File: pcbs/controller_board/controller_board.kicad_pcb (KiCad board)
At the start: 2 copper layers, 72 x 44 mm, 41 parts, among them J1 RJ45, J2 PINHD-1X7, J3 PINHD-1X12, J4 PINHD-1X4, P1 24V / 5A, Q1 220mA / 50V, Q2 220mA / 50V, U1 8-28V in / 5V 5W out, U2 Particle2 / Boron, U3 A: 1.2 to 3.3V B: 1.8 to 5.5V

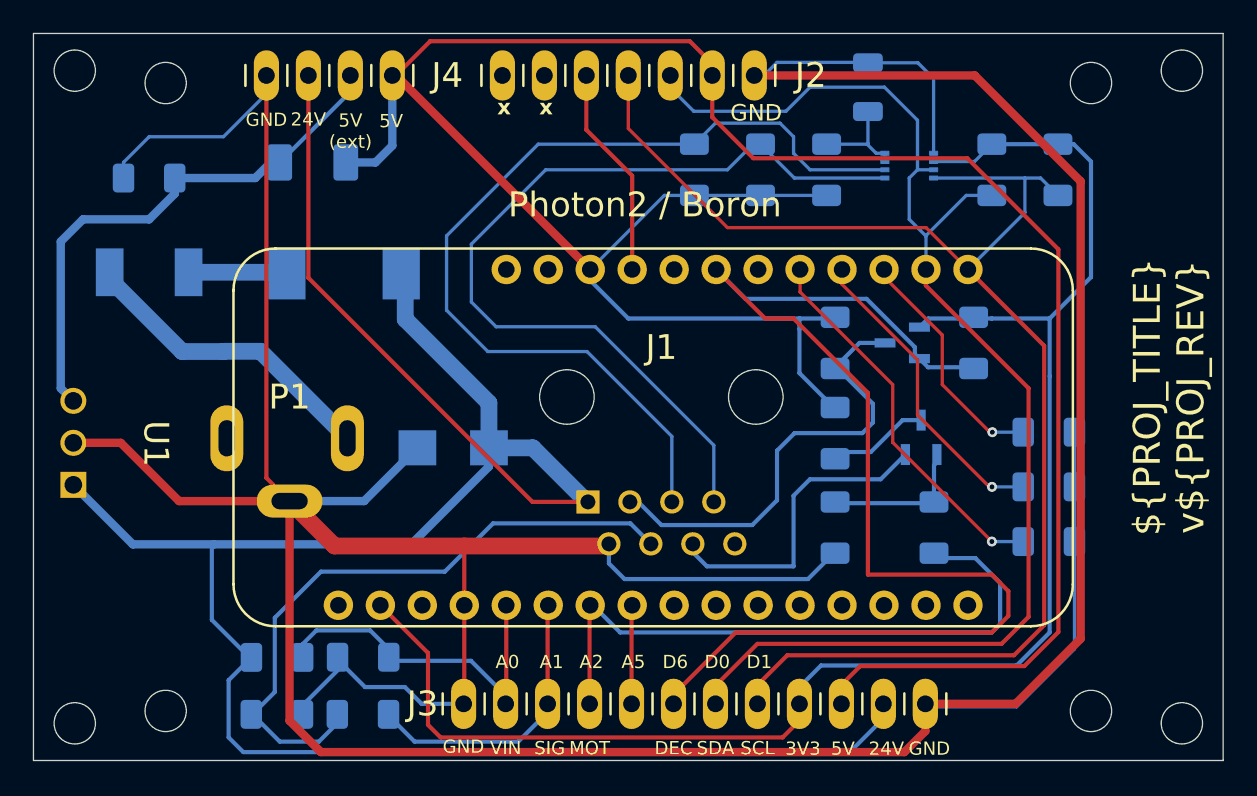
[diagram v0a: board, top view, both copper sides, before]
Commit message: update controller board to version 1.1 - i2c level shifting back to mosfets
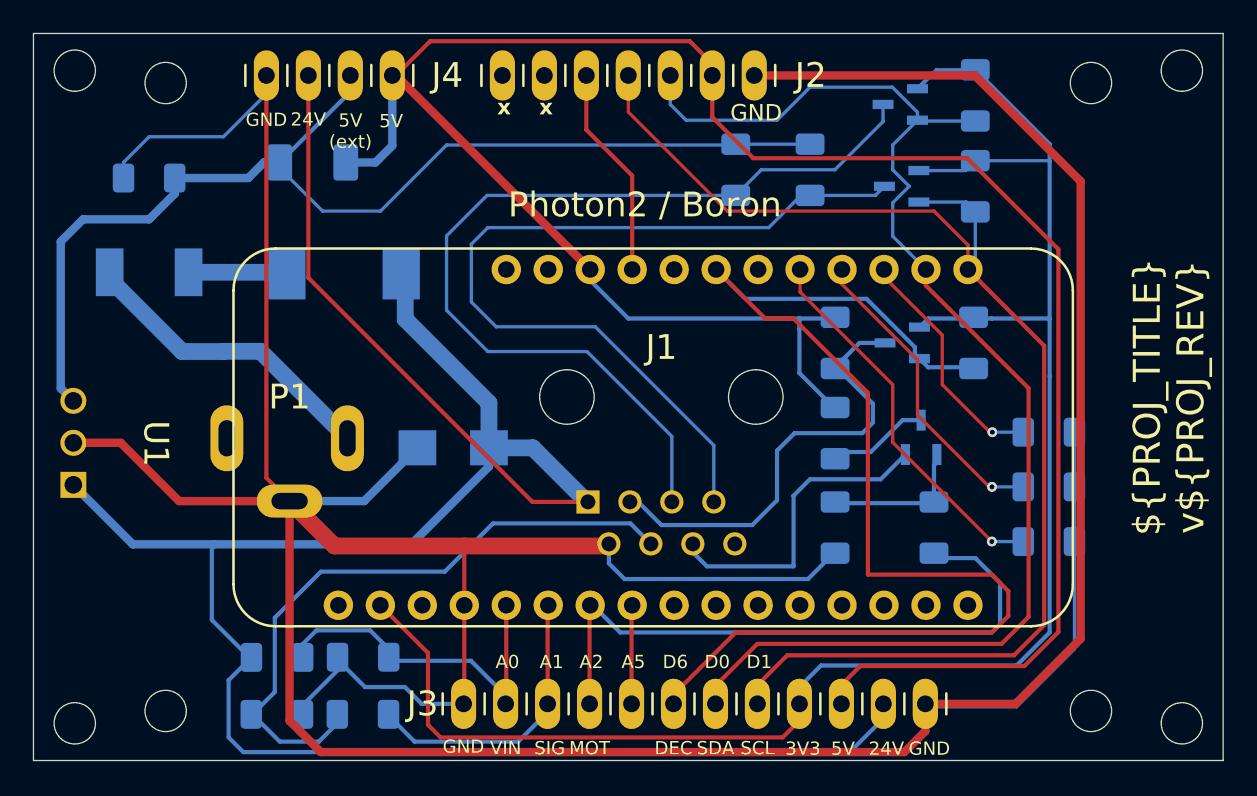
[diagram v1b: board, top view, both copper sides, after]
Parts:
- removed C1: 100pF, footprints:C_1206
- removed R15: 200kΩ, footprints:R_1206
- removed U3: A: 1.2 to 3.3V B: 1.8 to 5.5V, footprints:SOT-765-1_VSSOP8
- added Q3: 220mA / 50V, footprints:SOT-23-3, B.Cu at (152.5, 84.0)
- added Q4: 220mA / 50V, footprints:SOT-23-3, B.Cu at (152.5, 89.0)
- R11, R12, R13, R14: value 2.2kΩ -> 10kΩ
- moved R11 19.5 mm to (142.5, 88.0), turned to -90 degrees
- moved R14 13.0 mm to (157.0, 89.0), turned to 90 degrees
- moved R13 7.00 mm to (147.0, 88.0)
- moved R12 4.61 mm to (157.0, 83.5)
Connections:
- D2 pad 2: /Vout -> +5Vout
- J4 pad 3: /Vout -> +5Vout
- R11 pad 1: /D0-SDA -> +5Vout
- R11 pad 2: +3V3 -> /5V-SCL
- R13 pad 1: /5V-SCL -> +5Vout
- R13 pad 2: +5V -> /5V-SDA
- R14 pad 1: /5V-SDA -> /D0-SDA
- R14 pad 2: +5V -> +3V3
- R7 pad 1: /Vout -> +5Vout
- U1 pad 3: /Vout -> +5Vout
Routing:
- net +5Vout: track 0.00 -> 67.7 mm
- net /Vout: track 32.8 -> 0.00 mm
- net +5V: track 150.3 -> 134.2 mm
- net GND: track 277.2 -> 261.6 mm
- net +3V3: track 98.3 -> 106.4 mm
- net /D0-SDA: track 87.9 -> 80.7 mm
- net Net-(U3-EN): track 6.25 -> 0.00 mm
- net /5V-SDA: track 53.7 -> 52.5 mm
- net /5V-SCL: track 56.4 -> 55.6 mm
- net /D1-SCL: track 79.9 -> 80.4 mm

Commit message: use updated header symbols, otherwise no changes
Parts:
- J2: value PINHD-1X7 -> Conn_01x07
- J3: value PINHD-1X12 -> Conn_01x12
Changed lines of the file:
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@@
 	(net 37 "/S3")
 	(net 38 "/D3")
-	(net 39 "unconnected-(J2-Pad6)")
-	(net 40 "unconnected-(J2-Pad7)")
+	(net 39 "unconnected-(J2-Pin_6-Pad6)")
+	(net 40 "unconnected-(J2-Pin_7-Pad7)")
 	(net 41 "unconnected-(P1-Pad3)")
 	(net 42 "/A5")
@@
 			)
 		)
-		(property "Value" "PINHD-1X12"
+		(property "Value" "Conn_01x12"
 			(at -15.24 3.175 0)
 			(unlocked yes)
@@
 			)
 		)
-		(property "Datasheet" ""
+		(property "Datasheet" "~"
 			(at 0 0 0)
 			(layer "F.Fab")
@@
 			)
 		)
-		(property "Description" "PIN HEADER"
+		(property "Description" "Basic 0.1\" PTH"
 			(at 0 0 0)
 			(layer "F.Fab")
@@
 			)
 		)
+		(property ki_fp_filters "Connector*:*_1x??_*")
 		(sheetname "/")
 		(sheetfile "controller_board.kicad_sch")
@@
 			(remove_unused_layers no)
 			(net 1 "GND")
-			(pinfunction "1")
+			(pinfunction "Pin_1")
 			(pintype "passive")
 			(solder_mask_margin 0.1016)
@@
 			(remove_unused_layers no)
 			(net 4 "/A0-VIN")
-			(pinfunction "2")
+			(pinfunction "Pin_2")
 			(pintype "passive")
 			(solder_mask_margin 0.1016)
@@
 			(remove_unused_layers no)
 			(net 8 "/A1-SIGNAL")
-			(pinfunction "3")
+			(pinfunction "Pin_3")
 			(pintype "passive")
 			(solder_mask_margin 0.1016)
@@
 			(remove_unused_layers no)
 			(net 2 "/A2-MOTOR")
-			(pinfunction "4")
+			(pinfunction "Pin_4")
 			(pintype "passive")
 			(solder_mask_margin 0.1016)
@@
 			(remove_unused_layers no)
 			(net 42 "/A5")
-			(pinfunction "5")
+			(pinfunction "Pin_5")
 			(pintype "passive")
 			(solder_mask_margin 0.1016)
@@
 			(remove_unused_layers no)
 			(net 5 "/D6-DECO")
-			(pinfunction "6")
+			(pinfunction "Pin_6")
 			(pintype "passive")
 			(solder_mask_margin 0.1016)
@@
 			(remove_unused_layers no)
 			(net 3 "/D1-SCL")
-			(pinfunction "7")
+			(pinfunction "Pin_7")
 			(pintype "passive")
 			(solder_mask_margin 0.1016)
@@
 			(remove_unused_layers no)
 			(net 6 "/D0-SDA")
-			(pinfunction "8")
+			(pinfunction "Pin_8")
 			(pintype "passive")
 			(solder_mask_margin 0.1016)
@@
 			(remove_unused_layers no)
 			(net 19 "+3V3")
-			(pinfunction "9")
+			(pinfunction "Pin_9")
 			(pintype "passive")
 			(solder_mask_margin 0.1016)
@@
 			(remove_unused_layers no)
 			(net 17 "+5V")
-			(pinfunction "10")
+			(pinfunction "Pin_10")
 			(pintype "passive")
 			(solder_mask_margin 0.1016)
@@
 			(remove_unused_layers no)
 			(net 18 "+24V")
-			(pinfunction "11")
+			(pinfunction "Pin_11")
 			(pintype "passive")
 			(solder_mask_margin 0.1016)
@@
 			(remove_unused_layers no)
 			(net 1 "GND")
-			(pinfunction "12")
+			(pinfunction "Pin_12")
 			(pintype "passive")
 			(solder_mask_margin 0.1016)
@@
 			)
 		)
-		(property "Value" "PINHD-1X7"
+		(property "Value" "Conn_01x07"
 			(at -8.89 3.175 180)
 			(unlocked yes)
@@
 			)
 		)
-		(property "Datasheet" ""
+		(property "Datasheet" "~"
 			(at 0 0 180)
 			(layer "F.Fab")
@@
 			)
 		)
-		(property "Description" "PIN HEADER"
+		(property "Description" "Basic 0.1\" PTH"
 			(at 0 0 180)
 			(layer "F.Fab")
@@
 			)
 		)
+		(property ki_fp_filters "Connector*:*_1x??_*")
 		(sheetname "/")
 		(sheetfile "controller_board.kicad_sch")
@@
 			(remove_unused_layers no)
 			(net 1 "GND")
-			(pinfunction "1")
+			(pinfunction "Pin_1")
 			(pintype "passive")
 			(solder_mask_margin 0.1016)
@@
 			(remove_unused_layers no)
 			(net 17 "+5V")
-			(pinfunction "2")
+			(pinfunction "Pin_2")
 			(pintype "passive")
 			(solder_mask_margin 0.1016)
@@
 			(remove_unused_layers no)
 			(net 3 "/D1-SCL")
-			(pinfunction "3")
+			(pinfunction "Pin_3")
 			(pintype "passive")
 			(solder_mask_margin 0.1016)
@@
 			(remove_unused_layers no)
 			(net 6 "/D0-SDA")
-			(pinfunction "4")
+			(pinfunction "Pin_4")
 			(pintype "passive")
 			(solder_mask_margin 0.1016)
@@
 			(remove_unused_layers no)
 			(net 16 "/D10-RST")
-			(pinfunction "5")
+			(pinfunction "Pin_5")
 			(pintype "passive")
 			(solder_mask_margin 0.1016)
@@
 			(layers "*.Cu" "*.Mask")
 			(remove_unused_layers no)
-			(net 39 "unconnected-(J2-Pad6)")
-			(pinfunction "6")
+			(net 39 "unconnected-(J2-Pin_6-Pad6)")
+			(pinfunction "Pin_6")
 			(pintype "passive+no_connect")
 			(solder_mask_margin 0.1016)
@@
 			(layers "*.Cu" "*.Mask")
 			(remove_unused_layers no)
-			(net 40 "unconnected-(J2-Pad7)")
-			(pinfunction "7")
+			(net 40 "unconnected-(J2-Pin_7-Pad7)")
+			(pinfunction "Pin_7")
 			(pintype "passive+no_connect")
 			(solder_mask_margin 0.1016)
@@
 			)
 		)
-		(property "Datasheet" ""
+		(property "Datasheet" "~"
 			(at 0 0 0)
 			(layer "F.Fab")
@@
 			)
 		)
-		(property "Description" "PIN HEADER"
+		(property "Description" "Basic 0.1\" PTH"
 			(at 0 0 0)
 			(layer "F.Fab")
@@
 			)
 		)
+		(property ki_fp_filters "Connector*:*_1x??_*")
 		(sheetname "/")
 		(sheetfile "controller_board.kicad_sch")
@@
 			(remove_unused_layers no)
 			(net 1 "GND")
-			(pinfunction "1")
+			(pinfunction "Pin_1")
 			(pintype "passive")
 			(solder_mask_margin 0.1016)
@@
 			(remove_unused_layers no)
 			(net 18 "+24V")
-			(pinfunction "2")
+			(pinfunction "Pin_2")
 			(pintype "passive")
 			(solder_mask_margin 0.1016)
@@
 			(remove_unused_layers no)
 			(net 7 "+5Vout")
-			(pinfunction "3")
+			(pinfunction "Pin_3")
 			(pintype "passive")
 			(solder_mask_margin 0.1016)
@@
 			(remove_unused_layers no)
 			(net 17 "+5V")
-			(pinfunction "4")
+			(pinfunction "Pin_4")
 			(pintype "passive")
 			(solder_mask_margin 0.1016)

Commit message: add signal stabilizing capacitors to controller and sensor boards
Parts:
- added C1: 10nF, footprints:C_0603, B.Cu at (129.5, 117.3)
- moved R3 5.77 mm to (120.5, 121.0)
- moved R4 4.94 mm to (115.0, 121.0)
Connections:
- R3 pad 1: /SIGNAL -> /A1-SIGNAL
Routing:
- net /A1-SIGNAL: track 17.6 -> 26.0 mm
- net /SIGNAL: track 38.9 -> 32.0 mm
- net GND: track 261.6 -> 262.5 mm

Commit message: controller board version 1.2 (just the signal cap added)
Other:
- board text added: "GEOM.KOPFLAB.ORG"
- board text added: "Photon2"
- board text removed: "Photon2 / Boron"
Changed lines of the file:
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@@
 		(tenting front back)
 		(pcbplotparams
-			(layerselection 0x00000000_00000000_55555555_555d5550)
-			(plot_on_all_layers_selection 0x00000000_00000000_00002a8a_02aaaaaf)
+			(layerselection 0x00000000_00000000_55555555_555555d0)
+			(plot_on_all_layers_selection 0x00000000_00000000_0000000a_0202aaaf)
 			(disableapertmacros no)
 			(usegerberextensions no)
@@
 		)
 	)
-	(gr_text "Photon2 / Boron"
-		(at 137 91 0)
+	(gr_text "Photon2"
+		(at 139.462452 106.033092 0)
 		(layer "F.SilkS")
 		(effects
@@
 		)
 	)
+	(gr_text "GEOM.KOPFLAB.ORG"
+		(at 168.5 103 90)
+		(layer "F.SilkS")
+		(effects
+			(font
+				(size 2 2)
+				(thickness 0.2)
+			)
+			(justify bottom)
+		)
+	)
 	(gr_text "A5"
 		(at 136.303746 117.785095 0)
@@
 	)
 	(gr_text "${PROJ_TITLE}\nv${PROJ_REV}"
-		(at 170.9989 101.7464 90)
+		(at 141.5 91.5 0)
 		(layer "F.SilkS")
 		(effects
 			(font
-				(size 1.63576 1.63576)
-				(thickness 0.14224)
+				(size 2 2)
+				(thickness 0.2)
 			)
 			(justify bottom)
@@
 		(type orthogonal)
 		(locked yes)
-		(layer "Cmts.User")
+		(layer "Dwgs.User")
 		(pts
 			(xy 102.5 123.75) (xy 102.5 121.5)
@@
 			(locked yes)
 			(at 95.5 120 90)
-			(layer "Cmts.User")
+			(layer "Dwgs.User")
 			(effects
 				(font
-					(size 1 1)
-					(thickness 0.15)
+					(size 1.5 1.5)
+					(thickness 1.3)
 				)
 			)
@@
 		(type orthogonal)
 		(locked yes)
-		(layer "Cmts.User")
+		(layer "Dwgs.User")
 		(pts
 			(xy 168.965985 80.74318) (xy 168.965985 83.24318)
@@
 			(locked yes)
 			(at 175.692389 82.029078 270)
-			(layer "Cmts.User")
+			(layer "Dwgs.User")
 			(effects
 				(font
-					(size 1 1)
-					(thickness 0.15)
+					(size 1.5 1.5)
+					(thickness 1.3)
 				)
 			)
@@
 		(type orthogonal)
 		(locked yes)
-		(layer "Cmts.User")
+		(layer "Dwgs.User")
 		(pts
 			(xy 130.25 111.77) (xy 145.75 111.77)
@@
 			(locked yes)
 			(at 138.5 131.5 0)
-			(layer "Cmts.User")
+			(layer "Dwgs.User")
 			(effects
 				(font
-					(size 1 1)
-					(thickness 0.15)
+					(size 1.5 1.5)
+					(thickness 1.3)
 				)
 			)
@@
 		(type orthogonal)
 		(locked yes)
-		(layer "Cmts.User")
+		(layer "Dwgs.User")
 		(pts
 			(xy 100 121.5) (xy 102.5 121.5)
@@
 			(locked yes)
 			(at 103.284426 128.326075 0)
-			(layer "Cmts.User")
+			(layer "Dwgs.User")
 			(effects
 				(font
-					(size 1 1)
-					(thickness 0.15)
+					(size 1.5 1.5)
+					(thickness 1.3)
 				)
 			)
@@
 		(type orthogonal)
 		(locked yes)
-		(layer "Cmts.User")
+		(layer "Dwgs.User")
 		(pts
 			(xy 145.75 95.27) (xy 145.75 111.77)
@@
 			(locked yes)
 			(at 179.681035 104.067895 270)
-			(layer "Cmts.User")
+			(layer "Dwgs.User")
 			(effects
 				(font
-					(size 1 1)
-					(thickness 0.15)
+					(size 1.5 1.5)
+					(thickness 1.3)
 				)
 			)
@@
 		(type orthogonal)
 		(locked yes)
-		(layer "Cmts.User")
+		(layer "Dwgs.User")
 		(pts
 			(xy 164 122) (xy 164 119.5)
@@
 			(locked yes)
 			(at 175.5 120.5 270)
-			(layer "Cmts.User")
+			(layer "Dwgs.User")
 			(effects
 				(font
-					(size 1 1)
-					(thickness 0.15)
+					(size 1.5 1.5)
+					(thickness 1.3)
 				)
 			)
@@
 		(type orthogonal)
 		(locked yes)
-		(layer "Cmts.User")
+		(layer "Dwgs.User")
 		(pts
 			(xy 100 79.75) (xy 100 123.75)
@@
 			(locked yes)
 			(at 83.85 101.75 90)
-			(layer "Cmts.User")
+			(layer "Dwgs.User")
 			(effects
 				(font
-					(size 1 1)
-					(thickness 0.15)
+					(size 1.5 1.5)
+					(thickness 1.3)
 				)
 			)
@@
 		(type orthogonal)
 		(locked yes)
-		(layer "Cmts.User")
+		(layer "Dwgs.User")
 		(pts
 			(xy 108 120.75) (xy 100 121.5)
@@
 			(locked yes)
 			(at 104 131 0)
-			(layer "Cmts.User")
+			(layer "Dwgs.User")
 			(effects
 				(font
-					(size 1 1)
-					(thickness 0.15)
+					(size 1.5 1.5)
+					(thickness 1.3)
 				)
 			)
@@
 		(type orthogonal)
 		(locked yes)
-		(layer "Cmts.User")
+		(layer "Dwgs.User")
 		(pts
 			(xy 100 79.75) (xy 172 79.75)
@@
 			(locked yes)
 			(at 136 63.85 0)
-			(layer "Cmts.User")
+			(layer "Dwgs.User")
 			(effects
 				(font
-					(size 1 1)
-					(thickness 0.15)
+					(size 1.5 1.5)
+					(thickness 1.3)
 				)
 			)
@@
 		(type orthogonal)
 		(locked yes)
-		(layer "Cmts.User")
+		(layer "Dwgs.User")
 		(pts
 			(xy 108 123.75) (xy 108 120.75)
@@
 			(locked yes)
 			(at 91 121 90)
-			(layer "Cmts.User")
+			(layer "Dwgs.User")
 			(effects
 				(font
-					(size 1 1)
-					(thickness 0.15)
+					(size 1.5 1.5)
+					(thickness 1.3)
 				)
 			)
@@
 		(type orthogonal)
 		(locked yes)
-		(layer "Cmts.User")
+		(layer "Dwgs.User")
 		(pts
 			(xy 115.5 98.75) (xy 115.5 79.75)
@@
 		(gr_text "19 mm"
 			(locked yes)
-			(at 91.85 89.25 90)
-			(layer "Cmts.User")
+			(at 91.125 89.25 90)
+			(layer "Dwgs.User")
 			(effects
 				(font
-					(size 1 1)
-					(thickness 0.15)
+					(size 1.5 1.5)
+					(thickness 1.3)
 				)
 			)
@@
 		(type orthogonal)
 		(locked yes)
-		(layer "Cmts.User")
+		(layer "Dwgs.User")
 		(pts
 			(xy 145.5 123.75) (xy 145.75 111.77)
@@
 			(locked yes)
 			(at 179.761438 117.650327 270)
-			(layer "Cmts.User")
+			(layer "Dwgs.User")
 			(effects
 				(font
-					(size 1 1)
-					(thickness 0.15)
+					(size 1.5 1.5)
+					(thickness 1.3)
 				)
 			)
@@
 		(type orthogonal)
 		(locked yes)
-		(layer "Cmts.User")
+		(layer "Dwgs.User")
 		(pts
 			(xy 110 104.25) (xy 121 104.25)
@@
 		(gr_text "11 mm"
 			(locked yes)
-			(at 115.5 72.35 0)
-			(layer "Cmts.User")
+			(at 115.5 71.625 0)
+			(layer "Dwgs.User")
 			(effects
 				(font
-					(size 1 1)
-					(thickness 0.15)
+					(size 1.5 1.5)
+					(thickness 1.3)
 				)
 			)
@@
 		(type orthogonal)
 		(locked yes)
-		(layer "Cmts.User")
+		(layer "Dwgs.User")
 		(pts
 			(xy 145.75 111.77) (xy 172 112.103)
@@
 			(locked yes)
 			(at 159 131.5 0)
-			(layer "Cmts.User")
+			(layer "Dwgs.User")
 			(effects
 				(font
-					(size 1 1)
-					(thickness 0.15)
+					(size 1.5 1.5)
+					(thickness 1.3)
 				)
 			)
@@
 		(type orthogonal)
 		(locked yes)
-		(layer "Cmts.User")
+		(layer "Dwgs.User")
 		(pts
 			(xy 110 104.25) (xy 100 104.25)
@@
 		(gr_text "10 mm"
 			(locked yes)
-			(at 105 72.35 0)
-			(layer "Cmts.User")
+			(at 105 71.625 0)
+			(layer "Dwgs.User")
 			(effects
 				(font
-					(size 1 1)
-					(thickness 0.15)
+					(size 1.5 1.5)
+					(thickness 1.3)
 				)
 			)
